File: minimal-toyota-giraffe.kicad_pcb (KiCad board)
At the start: 2 copper layers, 39.4 x 24.1 mm, 6 parts, among them J1 USB_A, J2 MOBILEEYE, J3 MOBILEEYE, P1 panda, U1 Power

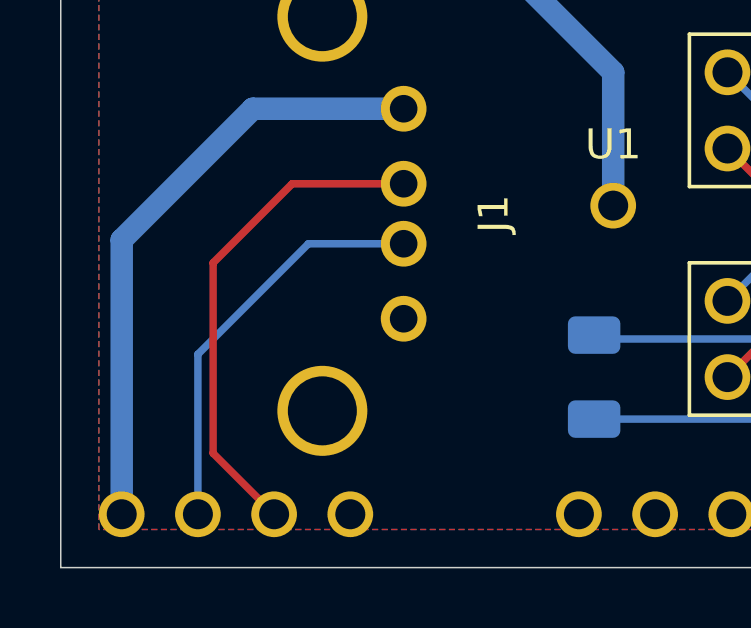
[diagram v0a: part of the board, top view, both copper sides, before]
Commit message: fixed USB D+ D- flip
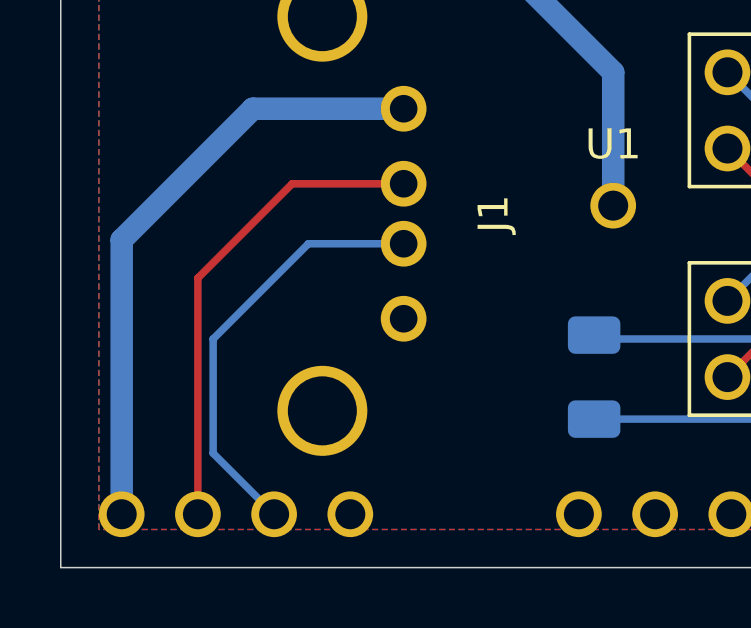
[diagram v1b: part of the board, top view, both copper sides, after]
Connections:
- P1 pad 10: (no net) -> Net-(P1-Pad10)
- P1 pad 16: (no net) -> Net-(P1-Pad16)
- P1 pad 18: (no net) -> Net-(P1-Pad18)
- P1 pad 19: (no net) -> Net-(P1-Pad19)
- P1 pad 2: Net-(J1-Pad3) -> Net-(J1-Pad2)
- P1 pad 3: Net-(J1-Pad2) -> Net-(J1-Pad3)
- P1 pad 5: (no net) -> Net-(P1-Pad5)
- P1 pad 6: (no net) -> Net-(P1-Pad6)
- P1 pad 7: (no net) -> Net-(P1-Pad7)
- P1 pad 9: (no net) -> Net-(P1-Pad9)
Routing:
- net Net-(J1-Pad3): track 13.7 -> 14.3 mm
- net Net-(J1-Pad2): track 16.7 -> 16.0 mm
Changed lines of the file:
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@@
-(kicad_pcb (version 20171130) (host pcbnew "(5.1.0)-1")
+(kicad_pcb (version 20171130) (host pcbnew "(5.1.2)-2")
   (general
     (thickness 1.6)
@@
     (zones 0)
     (modules 6)
-    (nets 15)
+    (nets 23)
   )
   (page A4)
@@
   (net 13 /CAN1_H')
   (net 14 /12VIN)
+  (net 15 "Net-(P1-Pad19)")
+  (net 16 "Net-(P1-Pad18)")
+  (net 17 "Net-(P1-Pad16)")
+  (net 18 "Net-(P1-Pad10)")
+  (net 19 "Net-(P1-Pad9)")
+  (net 20 "Net-(P1-Pad7)")
+  (net 21 "Net-(P1-Pad6)")
+  (net 22 "Net-(P1-Pad5)")
   (net_class Default "This is the default net class."
     (clearance 0.2)
@@
     (add_net "Net-(J1-Pad2)")
     (add_net "Net-(J1-Pad3)")
+    (add_net "Net-(P1-Pad10)")
+    (add_net "Net-(P1-Pad16)")
+    (add_net "Net-(P1-Pad18)")
+    (add_net "Net-(P1-Pad19)")
+    (add_net "Net-(P1-Pad5)")
+    (add_net "Net-(P1-Pad6)")
+    (add_net "Net-(P1-Pad7)")
+    (add_net "Net-(P1-Pad9)")
   )
   (module giraffe:panda (layer F.Cu)
@@
     (pad 20 thru_hole circle (at 27.94 -20.32) (size 1.524 1.524) (drill 1) (layers *.Cu *.Mask)
       (net 11 /CAN2_L))
-    (pad 19 thru_hole circle (at 25.4 -20.32) (size 1.524 1.524) (drill 1) (layers *.Cu *.Mask))
-    (pad 18 thru_hole circle (at 22.86 -20.32) (size 1.524 1.524) (drill 1) (layers *.Cu *.Mask))
+    (pad 19 thru_hole circle (at 25.4 -20.32) (size 1.524 1.524) (drill 1) (layers *.Cu *.Mask)
+      (net 15 "Net-(P1-Pad19)"))
+    (pad 18 thru_hole circle (at 22.86 -20.32) (size 1.524 1.524) (drill 1) (layers *.Cu *.Mask)
+      (net 16 "Net-(P1-Pad18)"))
     (pad 17 thru_hole circle (at 7.62 -20.32) (size 1.524 1.524) (drill 1) (layers *.Cu *.Mask)
       (net 5 /DFU))
-    (pad 16 thru_hole circle (at 5.08 -20.32) (size 1.524 1.524) (drill 1) (layers *.Cu *.Mask))
+    (pad 16 thru_hole circle (at 5.08 -20.32) (size 1.524 1.524) (drill 1) (layers *.Cu *.Mask)
+      (net 17 "Net-(P1-Pad16)"))
     (pad 15 thru_hole circle (at 2.54 -20.32) (size 1.524 1.524) (drill 1) (layers *.Cu *.Mask)
       (net 14 /12VIN))
@@
     (pad 11 thru_hole circle (at 30.48 0) (size 1.524 1.524) (drill 1) (layers *.Cu *.Mask)
       (net 9 /IGN))
-    (pad 10 thru_hole circle (at 27.94 0) (size 1.524 1.524) (drill 1) (layers *.Cu *.Mask))
-    (pad 9 thru_hole circle (at 25.4 0) (size 1.524 1.524) (drill 1) (layers *.Cu *.Mask))
+    (pad 10 thru_hole circle (at 27.94 0) (size 1.524 1.524) (drill 1) (layers *.Cu *.Mask)
+      (net 18 "Net-(P1-Pad10)"))
+    (pad 9 thru_hole circle (at 25.4 0) (size 1.524 1.524) (drill 1) (layers *.Cu *.Mask)
+      (net 19 "Net-(P1-Pad9)"))
     (pad 8 thru_hole circle (at 22.86 0) (size 1.524 1.524) (drill 1) (layers *.Cu *.Mask)
       (net 1 /GND))
-    (pad 7 thru_hole circle (at 20.32 0) (size 1.524 1.524) (drill 1) (layers *.Cu *.Mask))
-    (pad 6 thru_hole circle (at 17.78 0) (size 1.524 1.524) (drill 1) (layers *.Cu *.Mask))
-    (pad 5 thru_hole circle (at 15.24 0) (size 1.524 1.524) (drill 1) (layers *.Cu *.Mask))
+    (pad 7 thru_hole circle (at 20.32 0) (size 1.524 1.524) (drill 1) (layers *.Cu *.Mask)
+      (net 20 "Net-(P1-Pad7)"))
+    (pad 6 thru_hole circle (at 17.78 0) (size 1.524 1.524) (drill 1) (layers *.Cu *.Mask)
+      (net 21 "Net-(P1-Pad6)"))
+    (pad 5 thru_hole circle (at 15.24 0) (size 1.524 1.524) (drill 1) (layers *.Cu *.Mask)
+      (net 22 "Net-(P1-Pad5)"))
     (pad 4 thru_hole circle (at 7.62 0) (size 1.524 1.524) (drill 1) (layers *.Cu *.Mask)
       (net 1 /GND))
     (pad 3 thru_hole circle (at 5.08 0) (size 1.524 1.524) (drill 1) (layers *.Cu *.Mask)
+      (net 2 "Net-(J1-Pad3)"))
+    (pad 2 thru_hole circle (at 2.54 0) (size 1.524 1.524) (drill 1) (layers *.Cu *.Mask)
       (net 3 "Net-(J1-Pad2)"))
-    (pad 2 thru_hole circle (at 2.54 0) (size 1.524 1.524) (drill 1) (layers *.Cu *.Mask)
-      (net 2 "Net-(J1-Pad3)"))
     (pad 1 thru_hole circle (at 0 0) (size 1.524 1.524) (drill 1) (layers *.Cu *.Mask)
       (net 4 "Net-(J1-Pad1)"))
+  )
+  (module giraffe:USB (layer F.Cu)
+    (at 72.39 98.695 270)
+    (fp_text reference J1 (at 0 -3 270) (layer F.SilkS)
+      (effects (font (size 1 1) (thickness 0.15)))
+    )
+    (fp_text value USB_A (at 0 -4 270) (layer F.Fab)
+      (effects (font (size 1 1) (thickness 0.15)))
+    )
+    (pad 4 thru_hole circle (at 3.5 0 270) (size 1.524 1.524) (drill 0.92) (layers *.Cu *.Mask)
+      (net 1 /GND))
+    (pad 3 thru_hole circle (at 1 0 270) (size 1.524 1.524) (drill 0.92) (layers *.Cu *.Mask)
+      (net 2 "Net-(J1-Pad3)"))
+    (pad 2 thru_hole circle (at -1 0 270) (size 1.524 1.524) (drill 0.92) (layers *.Cu *.Mask)
+      (net 3 "Net-(J1-Pad2)"))
+    (pad 1 thru_hole circle (at -3.5 0 270) (size 1.524 1.524) (drill 0.92) (layers *.Cu *.Mask)
+      (net 4 "Net-(J1-Pad1)"))
+    (pad 5 thru_hole circle (at -6.57 2.71 270) (size 3 3) (drill 2.3) (layers *.Cu *.Mask)
+      (net 5 /DFU))
+    (pad ~ thru_hole circle (at 6.57 2.71 270) (size 3 3) (drill 2.3) (layers *.Cu *.Mask))
   )
   (module giraffe:12VIN (layer F.Cu)
@@
     (pad 1 thru_hole circle (at -6.35 -2.54) (size 1.524 1.524) (drill 1) (layers *.Cu *.Mask)
       (net 6 /HTR))
-  )
-  (module giraffe:USB (layer F.Cu)
-    (at 72.39 98.695 270)
-    (fp_text reference J1 (at 0 -3 270) (layer F.SilkS)
-      (effects (font (size 1 1) (thickness 0.15)))
-    )
-    (fp_text value USB_A (at 0 -4 270) (layer F.Fab)
-      (effects (font (size 1 1) (thickness 0.15)))
-    )
-    (pad 4 thru_hole circle (at 3.5 0 270) (size 1.524 1.524) (drill 0.92) (layers *.Cu *.Mask)
-      (net 1 /GND))
-    (pad 3 thru_hole circle (at 1 0 270) (size 1.524 1.524) (drill 0.92) (layers *.Cu *.Mask)
-      (net 2 "Net-(J1-Pad3)"))
-    (pad 2 thru_hole circle (at -1 0 270) (size 1.524 1.524) (drill 0.92) (layers *.Cu *.Mask)
-      (net 3 "Net-(J1-Pad2)"))
-    (pad 1 thru_hole circle (at -3.5 0 270) (size 1.524 1.524) (drill 0.92) (layers *.Cu *.Mask)
-      (net 4 "Net-(J1-Pad1)"))
-    (pad 5 thru_hole circle (at -6.57 2.71 270) (size 3 3) (drill 2.3) (layers *.Cu *.Mask)
-      (net 5 /DFU))
-    (pad ~ thru_hole circle (at 6.57 2.71 270) (size 3 3) (drill 2.3) (layers *.Cu *.Mask))
   )
   (module Resistor_SMD:R_1206_3216Metric (layer B.Cu)
@@
   (segment (start 90.805 96.52) (end 89.535 97.79) (width 0.75) (layer F.Cu) (net 1))
   (segment (start 90.805 96.52) (end 88.265 93.98) (width 0.75) (layer F.Cu) (net 1))
-  (segment (start 65.532 108.712) (end 65.532 103.378) (width 0.25) (layer B.Cu) (net 2))
   (segment (start 69.215 99.695) (end 72.39 99.695) (width 0.25) (layer B.Cu) (net 2))
-  (segment (start 65.532 103.378) (end 69.215 99.695) (width 0.25) (layer B.Cu) (net 2))
-  (segment (start 66.04 106.68) (end 66.04 100.33) (width 0.25) (layer F.Cu) (net 3))
-  (segment (start 68.072 108.712) (end 66.04 106.68) (width 0.25) (layer F.Cu) (net 3))
-  (segment (start 68.675 97.695) (end 72.39 97.695) (width 0.25) (layer F.Cu) (net 3))
-  (segment (start 66.04 100.33) (end 68.675 97.695) (width 0.25) (layer F.Cu) (net 3))
+  (segment (start 66.04 102.87) (end 69.215 99.695) (width 0.25) (layer B.Cu) (net 2))
+  (segment (start 68.072 108.712) (end 66.04 106.68) (width 0.25) (layer B.Cu) (net 2))
+  (segment (start 66.04 106.68) (end 66.04 102.87) (width 0.25) (layer B.Cu) (net 2))
+  (segment (start 72.39 97.695) (end 68.675 97.695) (width 0.25) (layer F.Cu) (net 3))
+  (segment (start 65.532 100.838) (end 65.532 108.712) (width 0.25) (layer F.Cu) (net 3))
+  (segment (start 68.675 97.695) (end 65.532 100.838) (width 0.25) (layer F.Cu) (net 3))
   (segment (start 62.992 99.568) (end 62.992 108.712) (width 0.75) (layer B.Cu) (net 4))
   (segment (start 72.39 95.195) (end 67.365 95.195) (width 0.75) (layer B.Cu) (net 4))

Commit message: new board design
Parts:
- removed J1: USB_A, giraffe:USB
- added JP1: Paw_Boot, Jumper:SolderJumper-2_P1.3mm_Open_RoundedPad1.0x1.5mm, B.Cu at (116.8, 80.0)
- added U2: USB, giraffe:USB, F.Cu at (102.9, 89.9)
- R1: moved to F.Cu
- moved R1 61.7 mm to (139.8, 95.2), turned to 180 degrees
- moved U1 47.1 mm to (125.7, 90.2), turned to 270 degrees
- moved J2 45.4 mm to (134.6, 91.4)
- moved P1 44.0 mm to (106.1, 99.8)
- moved J3 26.9 mm to (111.8, 88.9), turned to 180 degrees
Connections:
- P1 pad 10: Net-(P1-Pad10) -> (no net)
- P1 pad 16: Net-(P1-Pad16) -> (no net)
- P1 pad 18: Net-(P1-Pad18) -> (no net)
- P1 pad 19: Net-(P1-Pad19) -> (no net)
- P1 pad 5: Net-(P1-Pad5) -> (no net)
- P1 pad 6: Net-(P1-Pad6) -> (no net)
- P1 pad 7: Net-(P1-Pad7) -> (no net)
- P1 pad 9: Net-(P1-Pad9) -> (no net)
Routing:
- net /GND: track 23.1 -> 0.00 mm, vias 0 -> 14
- net /4: track 0.00 -> 22.0 mm
- net /CAN2_H: track 21.3 -> 42.4 mm, vias 0 -> 1
- net /CAN2_L: track 26.3 -> 46.9 mm, vias 1 -> 0
- net /9: track 0.00 -> 16.5 mm
- net /3: track 0.00 -> 16.5 mm
- net /CAN1_H': track 24.1 -> 38.8 mm
- net /CAN1_L': track 22.3 -> 36.8 mm, vias 1 -> 0
- net Net-(JP1-Pad1): track 20.4 -> 32.2 mm
- net /8: track 0.00 -> 11.1 mm
- net /2: track 0.00 -> 11.1 mm
- net /HTR: track 9.20 -> 5.08 mm
- net /CAN1_H: track 7.74 -> 11.3 mm
- net /IGN: track 20.3 -> 16.9 mm
- net /12VIN: track 20.6 -> 23.7 mm
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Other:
- board size 39.4 x 24.1 mm -> 42.5 x 24.1 mm
